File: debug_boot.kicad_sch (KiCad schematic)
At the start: 11 parts, among them J1 61300311121, J2 61300511121, J3 Conn_ARM_JTAG_SWD_10, J4 61300311121, J5 61300311121

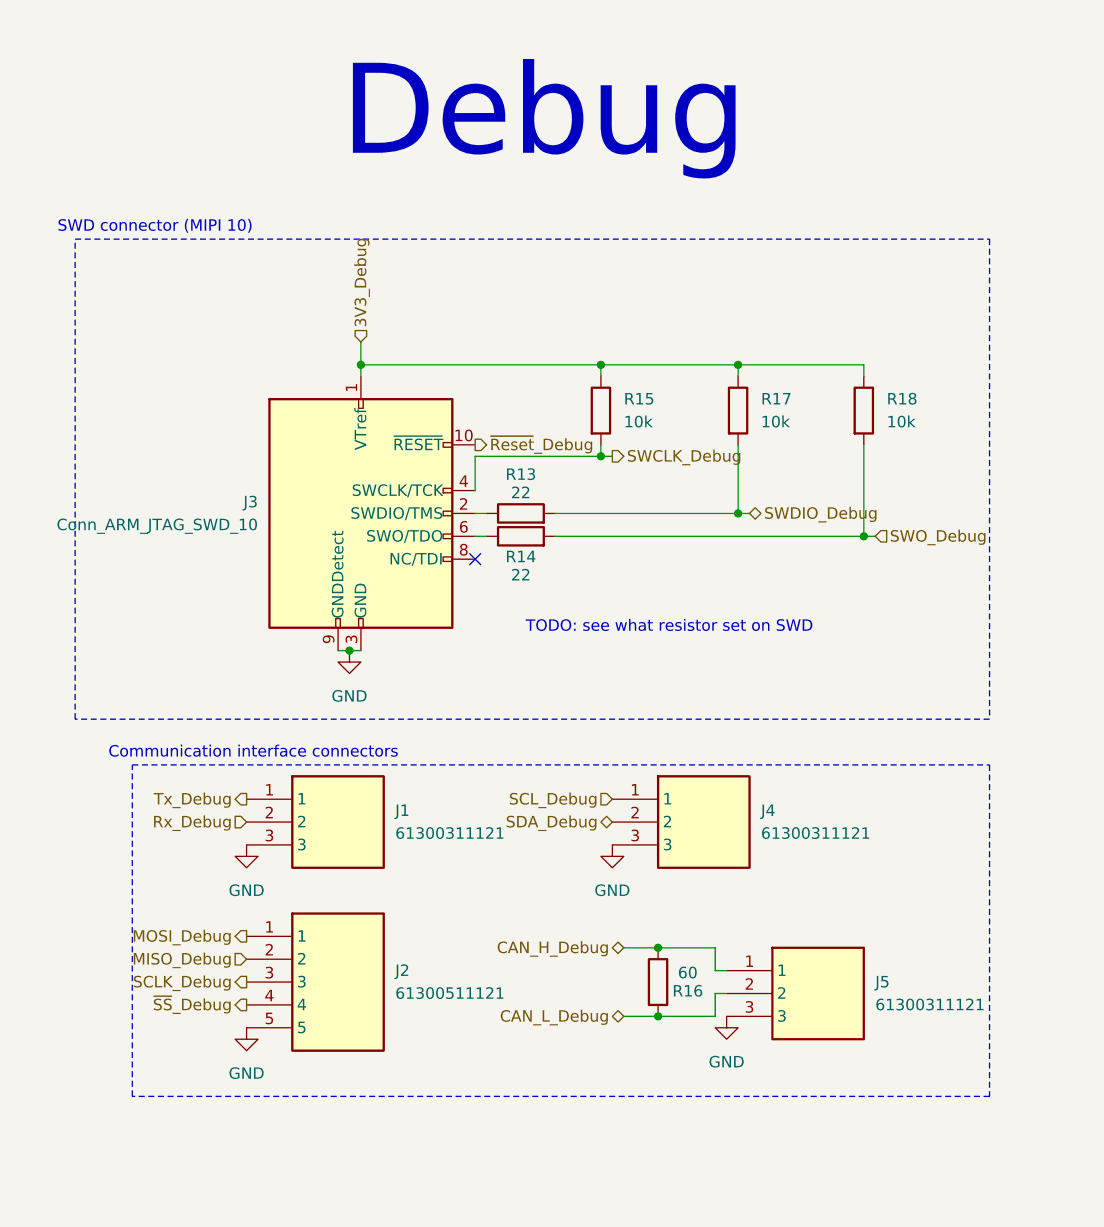
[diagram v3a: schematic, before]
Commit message: Reorder components number
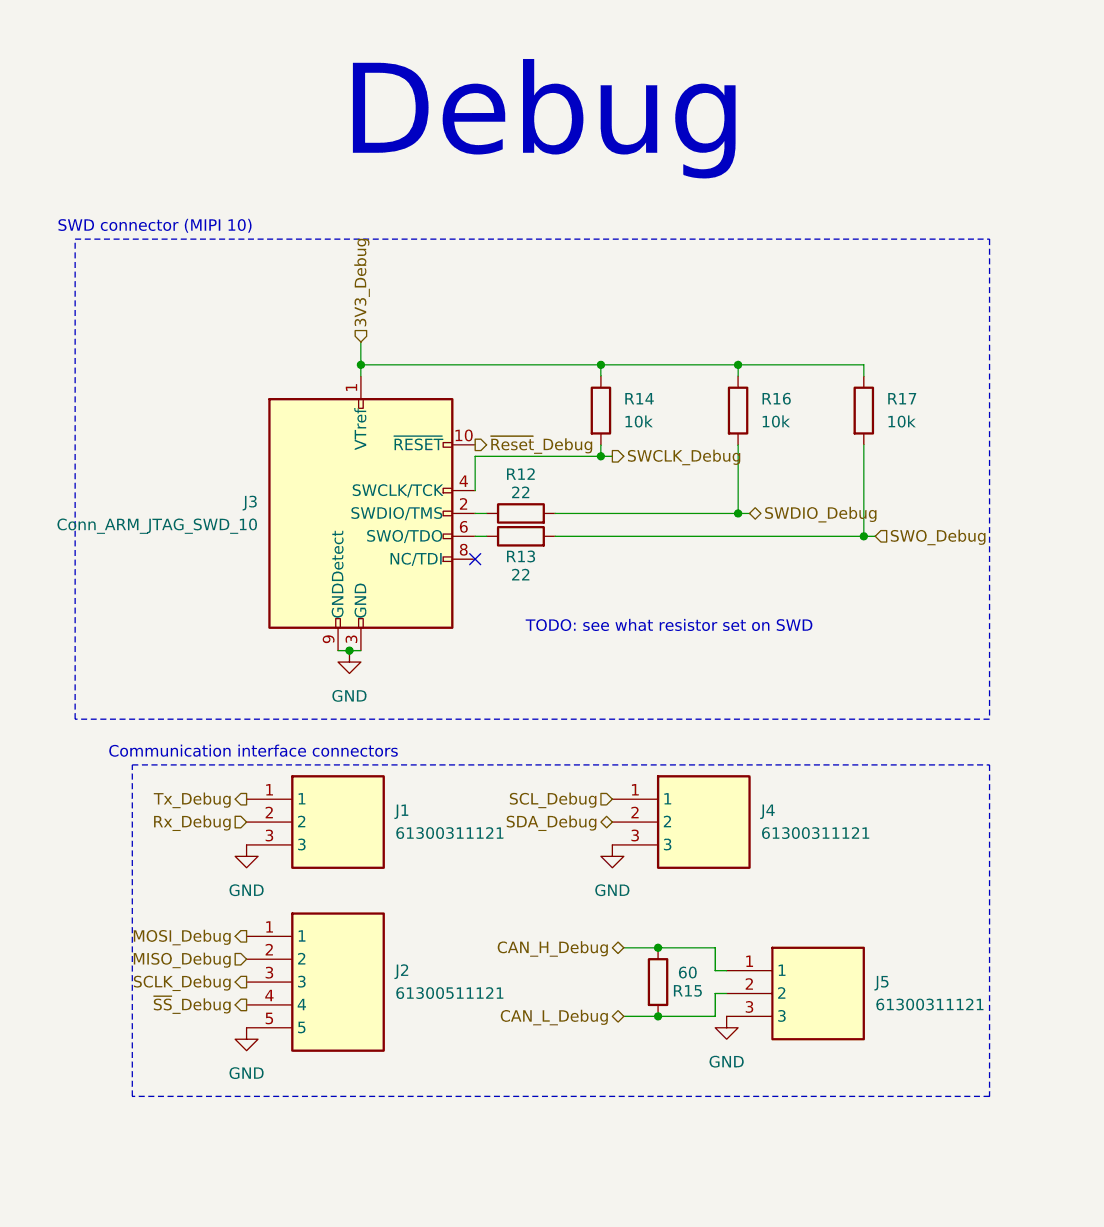
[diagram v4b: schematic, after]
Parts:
- renumbered R13 to R12, R14 to R13, R15 to R14, R16 to R15, R17 to R16, R18 to R17
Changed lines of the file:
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@@
 		(on_board yes)
 		(dnp no)
-		(property "Reference" "R16"
+		(property "Reference" "R15"
 			(at 168.402 122.936 0)
 			(effects
@@
 			(project "weather-station-poc"
 				(path "/38eb53bb-294e-46e4-ad59-fd355ca373b9/8a588a02-5ba4-4712-b770-7d9eb4e5d127"
-					(reference "R16")
+					(reference "R15")
 					(unit 1)
 				)
@@
 		(on_board yes)
 		(dnp no)
-		(property "Reference" "R14"
+		(property "Reference" "R13"
 			(at 149.86 74.676 90)
 			(effects
@@
 			(project ""
 				(path "/38eb53bb-294e-46e4-ad59-fd355ca373b9/8a588a02-5ba4-4712-b770-7d9eb4e5d127"
-					(reference "R14")
+					(reference "R13")
 					(unit 1)
 				)
@@
 		(dnp no)
 		(fields_autoplaced yes)
-		(property "Reference" "#PWR0121"
+		(property "Reference" "#PWR0111"
 			(at 172.72 132.08 0)
 			(effects
@@
 			(project "weather-station-poc"
 				(path "/38eb53bb-294e-46e4-ad59-fd355ca373b9/8a588a02-5ba4-4712-b770-7d9eb4e5d127"
-					(reference "#PWR0121")
+					(reference "#PWR0111")
 					(unit 1)
 				)
@@
 		(dnp no)
 		(fields_autoplaced yes)
-		(property "Reference" "R17"
+		(property "Reference" "R16"
 			(at 176.53 57.1499 0)
 			(effects
@@
 			(project "weather-station-poc"
 				(path "/38eb53bb-294e-46e4-ad59-fd355ca373b9/8a588a02-5ba4-4712-b770-7d9eb4e5d127"
-					(reference "R17")
+					(reference "R16")
 					(unit 1)
 				)
@@
 		(on_board yes)
 		(dnp no)
-		(property "Reference" "R13"
+		(property "Reference" "R12"
 			(at 149.86 65.532 90)
 			(effects
@@
 			(project "weather-station-poc"
 				(path "/38eb53bb-294e-46e4-ad59-fd355ca373b9/8a588a02-5ba4-4712-b770-7d9eb4e5d127"
-					(reference "R13")
+					(reference "R12")
 					(unit 1)
 				)
@@
 		(dnp no)
 		(fields_autoplaced yes)
-		(property "Reference" "R15"
+		(property "Reference" "R14"
 			(at 161.29 57.1499 0)
 			(effects
@@
 			(project ""
 				(path "/38eb53bb-294e-46e4-ad59-fd355ca373b9/8a588a02-5ba4-4712-b770-7d9eb4e5d127"
-					(reference "R15")
+					(reference "R14")
 					(unit 1)
 				)
@@
 		(dnp no)
 		(fields_autoplaced yes)
-		(property "Reference" "#PWR0118"
+		(property "Reference" "#PWR0108"
 			(at 119.38 133.35 0)
 			(effects
@@
 			(project "weather-station-poc"
 				(path "/38eb53bb-294e-46e4-ad59-fd355ca373b9/8a588a02-5ba4-4712-b770-7d9eb4e5d127"
-					(reference "#PWR0118")
+					(reference "#PWR0108")
 					(unit 1)
 				)
@@
 		(dnp no)
 		(fields_autoplaced yes)
-		(property "Reference" "#PWR0120"
+		(property "Reference" "#PWR0110"
 			(at 160.02 113.03 0)
 			(effects
@@
 			(project "weather-station-poc"
 				(path "/38eb53bb-294e-46e4-ad59-fd355ca373b9/8a588a02-5ba4-4712-b770-7d9eb4e5d127"
-					(reference "#PWR0120")
+					(reference "#PWR0110")
 					(unit 1)
 				)
@@
 		(dnp no)
 		(fields_autoplaced yes)
-		(property "Reference" "R18"
+		(property "Reference" "R17"
 			(at 190.5 57.1499 0)
 			(effects
@@
 			(project "weather-station-poc"
 				(path "/38eb53bb-294e-46e4-ad59-fd355ca373b9/8a588a02-5ba4-4712-b770-7d9eb4e5d127"
-					(reference "R18")
+					(reference "R17")
 					(unit 1)
 				)
@@
 		(dnp no)
 		(fields_autoplaced yes)
-		(property "Reference" "#PWR0117"
+		(property "Reference" "#PWR0107"
 			(at 119.38 113.03 0)
 			(effects
@@
 			(project ""
 				(path "/38eb53bb-294e-46e4-ad59-fd355ca373b9/8a588a02-5ba4-4712-b770-7d9eb4e5d127"
-					(reference "#PWR0117")
+					(reference "#PWR0107")
 					(unit 1)
 				)
@@
 		(dnp no)
 		(fields_autoplaced yes)
-		(property "Reference" "#PWR0119"
+		(property "Reference" "#PWR0109"
 			(at 130.81 91.44 0)
 			(effects
@@
 			(project ""
 				(path "/38eb53bb-294e-46e4-ad59-fd355ca373b9/8a588a02-5ba4-4712-b770-7d9eb4e5d127"
-					(reference "#PWR0119")
-					(unit 1)
-				)
+					(reference "#PWR0109")
+					(unit 1)
+				)

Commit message: Assign 0603 footprints to all resistors
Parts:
- R12, R13, R14, R15, R16, R17: footprint (none) -> Resistor_SMD:R_0603_1608Metric_Pad0.98x0.95mm_HandSolder
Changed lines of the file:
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@@
 			)
 		)
-		(property "Footprint" ""
+		(property "Footprint" "Resistor_SMD:R_0603_1608Metric_Pad0.98x0.95mm_HandSolder"
 			(at 163.322 121.92 90)
 			(effects
@@
 			)
 		)
-		(property "Footprint" ""
+		(property "Footprint" "Resistor_SMD:R_0603_1608Metric_Pad0.98x0.95mm_HandSolder"
 			(at 149.86 74.168 90)
 			(effects
@@
 			)
 		)
-		(property "Footprint" ""
+		(property "Footprint" "Resistor_SMD:R_0603_1608Metric_Pad0.98x0.95mm_HandSolder"
 			(at 172.212 58.42 90)
 			(effects
@@
 			)
 		)
-		(property "Footprint" ""
+		(property "Footprint" "Resistor_SMD:R_0603_1608Metric_Pad0.98x0.95mm_HandSolder"
 			(at 149.86 71.628 90)
 			(effects
@@
 			)
 		)
-		(property "Footprint" ""
+		(property "Footprint" "Resistor_SMD:R_0603_1608Metric_Pad0.98x0.95mm_HandSolder"
 			(at 156.972 58.42 90)
 			(effects
@@
 			)
 		)
-		(property "Footprint" ""
+		(property "Footprint" "Resistor_SMD:R_0603_1608Metric_Pad0.98x0.95mm_HandSolder"
 			(at 186.182 58.42 90)
 			(effects

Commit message: Fill the cartridge for all schematics
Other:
- company: (none) -> Julien Cruvieux
- title: (none) -> Debug
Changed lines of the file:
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@@
 	(generator_version "9.0")
 	(paper "A4")
+	(title_block
+		(title "Debug")
+		(date "2025-12-26")
+		(rev "A")
+		(company "Julien Cruvieux")
+	)
 	(rectangle
 		(start 100.33 39.37)

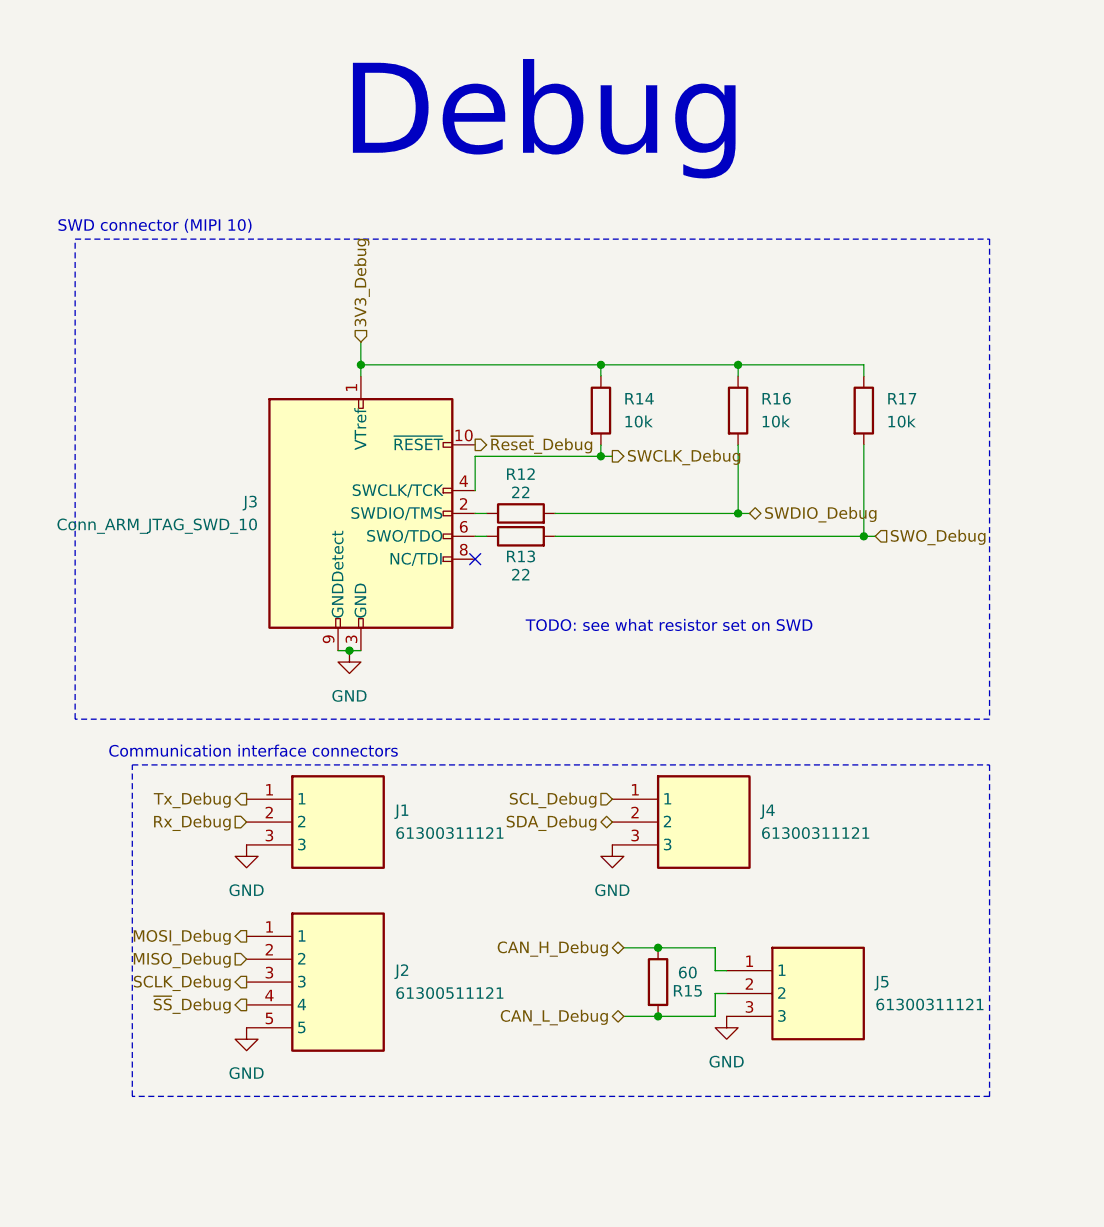
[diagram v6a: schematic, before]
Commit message: Components reindexing and update of PCB
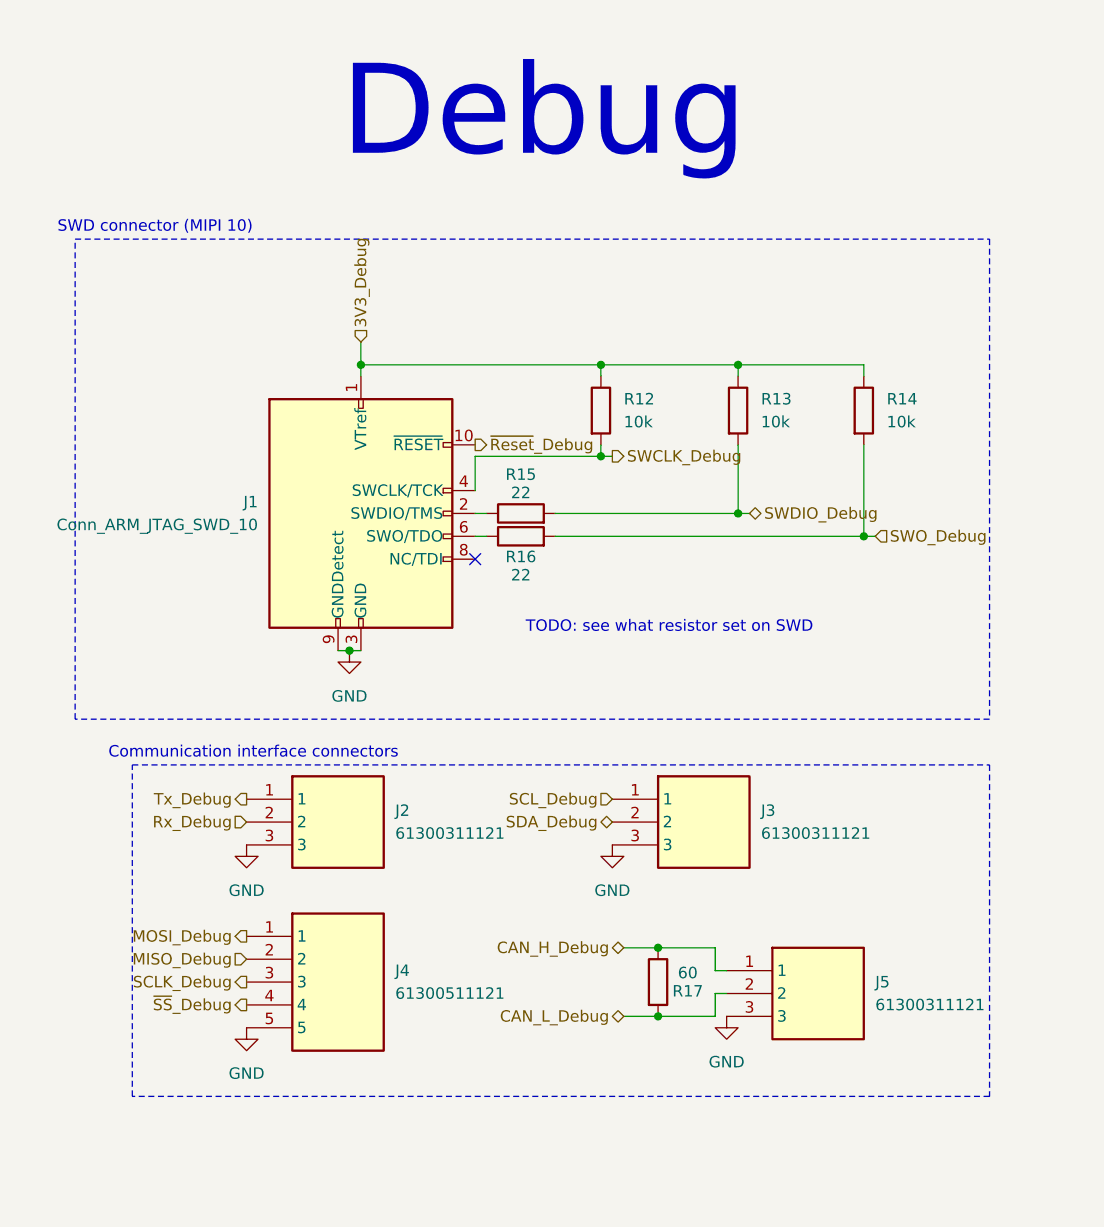
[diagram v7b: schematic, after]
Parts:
- renumbered J3 to J1, J1 to J2, J4 to J3, J2 to J4, R14 to R12, R16 to R13, R17 to R14, R12 to R15, R13 to R16, R15 to R17
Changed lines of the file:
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@@
 		(on_board yes)
 		(dnp no)
-		(property "Reference" "R15"
+		(property "Reference" "R17"
 			(at 168.402 122.936 0)
 			(effects
@@
 			(project "weather-station-poc"
 				(path "/38eb53bb-294e-46e4-ad59-fd355ca373b9/8a588a02-5ba4-4712-b770-7d9eb4e5d127"
-					(reference "R15")
+					(reference "R17")
 					(unit 1)
 				)
@@
 		(dnp no)
 		(fields_autoplaced yes)
-		(property "Reference" "J4"
+		(property "Reference" "J3"
 			(at 176.53 102.8699 0)
 			(effects
@@
 			(project "weather-station-poc"
 				(path "/38eb53bb-294e-46e4-ad59-fd355ca373b9/8a588a02-5ba4-4712-b770-7d9eb4e5d127"
-					(reference "J4")
+					(reference "J3")
 					(unit 1)
 				)
@@
 		(dnp no)
 		(fields_autoplaced yes)
-		(property "Reference" "J1"
+		(property "Reference" "J2"
 			(at 135.89 102.8699 0)
 			(effects
@@
 			(project ""
 				(path "/38eb53bb-294e-46e4-ad59-fd355ca373b9/8a588a02-5ba4-4712-b770-7d9eb4e5d127"
-					(reference "J1")
+					(reference "J2")
 					(unit 1)
 				)
@@
 		(dnp no)
 		(fields_autoplaced yes)
-		(property "Reference" "J2"
+		(property "Reference" "J4"
 			(at 135.89 120.6499 0)
 			(effects
@@
 			(project ""
 				(path "/38eb53bb-294e-46e4-ad59-fd355ca373b9/8a588a02-5ba4-4712-b770-7d9eb4e5d127"
-					(reference "J2")
+					(reference "J4")
 					(unit 1)
 				)
@@
 		(on_board yes)
 		(dnp no)
-		(property "Reference" "R13"
+		(property "Reference" "R16"
 			(at 149.86 74.676 90)
 			(effects
@@
 			(project ""
 				(path "/38eb53bb-294e-46e4-ad59-fd355ca373b9/8a588a02-5ba4-4712-b770-7d9eb4e5d127"
-					(reference "R13")
+					(reference "R16")
 					(unit 1)
 				)
@@
 		(dnp no)
 		(fields_autoplaced yes)
-		(property "Reference" "#PWR0111"
+		(property "Reference" "#PWR0110"
 			(at 172.72 132.08 0)
 			(effects
@@
 			(project "weather-station-poc"
 				(path "/38eb53bb-294e-46e4-ad59-fd355ca373b9/8a588a02-5ba4-4712-b770-7d9eb4e5d127"
-					(reference "#PWR0111")
+					(reference "#PWR0110")
 					(unit 1)
 				)
@@
 		(dnp no)
 		(fields_autoplaced yes)
-		(property "Reference" "R16"
+		(property "Reference" "R13"
 			(at 176.53 57.1499 0)
 			(effects
@@
 			(project "weather-station-poc"
 				(path "/38eb53bb-294e-46e4-ad59-fd355ca373b9/8a588a02-5ba4-4712-b770-7d9eb4e5d127"
-					(reference "R16")
+					(reference "R13")
 					(unit 1)
 				)
@@
 		(on_board yes)
 		(dnp no)
-		(property "Reference" "R12"
+		(property "Reference" "R15"
 			(at 149.86 65.532 90)
 			(effects
@@
 			(project "weather-station-poc"
 				(path "/38eb53bb-294e-46e4-ad59-fd355ca373b9/8a588a02-5ba4-4712-b770-7d9eb4e5d127"
-					(reference "R12")
+					(reference "R15")
 					(unit 1)
 				)
@@
 		(dnp no)
 		(fields_autoplaced yes)
-		(property "Reference" "R14"
+		(property "Reference" "R12"
 			(at 161.29 57.1499 0)
 			(effects
@@
 			(project ""
 				(path "/38eb53bb-294e-46e4-ad59-fd355ca373b9/8a588a02-5ba4-4712-b770-7d9eb4e5d127"
-					(reference "R14")
+					(reference "R12")
 					(unit 1)
 				)
@@
 		(dnp no)
 		(fields_autoplaced yes)
-		(property "Reference" "J3"
+		(property "Reference" "J1"
 			(at 120.65 68.5799 0)
 			(effects
@@
 			(project "weather-station-poc"
 				(path "/38eb53bb-294e-46e4-ad59-fd355ca373b9/8a588a02-5ba4-4712-b770-7d9eb4e5d127"
-					(reference "J3")
+					(reference "J1")
 					(unit 1)
 				)
@@
 		(dnp no)
 		(fields_autoplaced yes)
-		(property "Reference" "#PWR0108"
+		(property "Reference" "#PWR0111"
 			(at 119.38 133.35 0)
 			(effects
@@
 			(project "weather-station-poc"
 				(path "/38eb53bb-294e-46e4-ad59-fd355ca373b9/8a588a02-5ba4-4712-b770-7d9eb4e5d127"
-					(reference "#PWR0108")
+					(reference "#PWR0111")
 					(unit 1)
 				)
@@
 		(dnp no)
 		(fields_autoplaced yes)
-		(property "Reference" "#PWR0110"
+		(property "Reference" "#PWR0109"
 			(at 160.02 113.03 0)
 			(effects
@@
 			(project "weather-station-poc"
 				(path "/38eb53bb-294e-46e4-ad59-fd355ca373b9/8a588a02-5ba4-4712-b770-7d9eb4e5d127"
-					(reference "#PWR0110")
+					(reference "#PWR0109")
 					(unit 1)
 				)
@@
 		(dnp no)
 		(fields_autoplaced yes)
-		(property "Reference" "R17"
+		(property "Reference" "R14"
 			(at 190.5 57.1499 0)
 			(effects
@@
 			(project "weather-station-poc"
 				(path "/38eb53bb-294e-46e4-ad59-fd355ca373b9/8a588a02-5ba4-4712-b770-7d9eb4e5d127"
-					(reference "R17")
+					(reference "R14")
 					(unit 1)
 				)
@@
 		(dnp no)
 		(fields_autoplaced yes)
-		(property "Reference" "#PWR0107"
+		(property "Reference" "#PWR0108"
 			(at 119.38 113.03 0)
 			(effects
@@
 			(project ""
 				(path "/38eb53bb-294e-46e4-ad59-fd355ca373b9/8a588a02-5ba4-4712-b770-7d9eb4e5d127"
-					(reference "#PWR0107")
+					(reference "#PWR0108")
 					(unit 1)
 				)
@@
 		(dnp no)
 		(fields_autoplaced yes)
-		(property "Reference" "#PWR0109"
+		(property "Reference" "#PWR0107"
 			(at 130.81 91.44 0)
 			(effects
@@
 			(project ""
 				(path "/38eb53bb-294e-46e4-ad59-fd355ca373b9/8a588a02-5ba4-4712-b770-7d9eb4e5d127"
-					(reference "#PWR0109")
-					(unit 1)
-				)
+					(reference "#PWR0107")
+					(unit 1)
+				)
